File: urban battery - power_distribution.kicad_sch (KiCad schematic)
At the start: 19 parts, among them J1 FRONT_ACC_OUT, J2 12V_IN, J3 12VHC_OUT_EXTRA, J4 TEL_OUT, J5 REAR_ACC_OUT, J6 MTR_CTRL_OUT, J7 12VLC_OUT_EXTRA, J8 12VLC_OUT_EXTRA, J9 12VLC_OUT_EXTRA

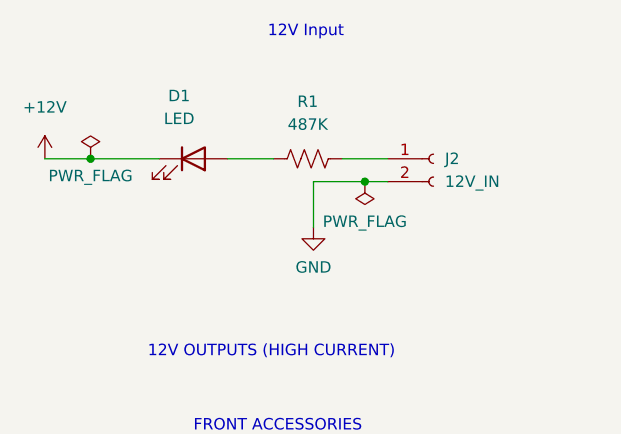
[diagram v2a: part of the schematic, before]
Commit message: fixed issue od 12V input going through LED
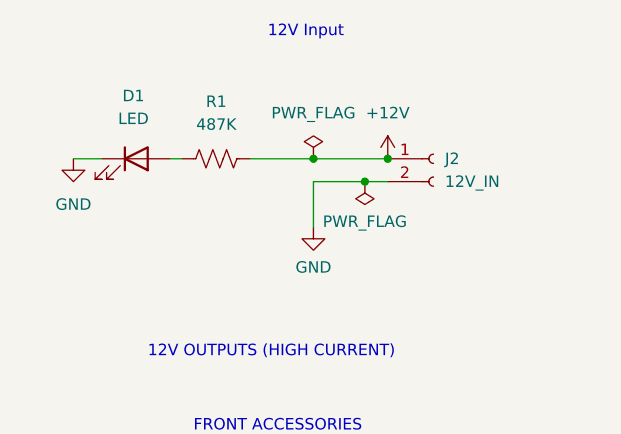
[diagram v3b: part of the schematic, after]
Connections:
- net +12V: now also J2.1 (Pin_1), R1.2; no longer D1.1 (K)
- net GND: now also D1.1 (K)
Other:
- moved on the sheet: D1, R1
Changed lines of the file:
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@@
 (kicad_sch (version 20211123) (generator eeschema)
   (paper "A4")
+  (junction (at 70.485 59.69) (diameter 0) (color 0 0 0 0)
+  )
   (junction (at 76.2 62.23) (diameter 0) (color 0 0 0 0)
   )
-  (junction (at 45.72 59.69) (diameter 0) (color 0 0 0 0)
+  (junction (at 78.74 59.69) (diameter 0) (color 0 0 0 0)
   )
   (wire (pts (xy 144.145 131.445) (xy 140.97 131.445))
@@
     (stroke (width 0) (type default) (color 0 0 0 0))
   )
-  (wire (pts (xy 73.66 59.69) (xy 78.74 59.69))
+  (wire (pts (xy 43.815 59.69) (xy 46.99 59.69))
     (stroke (width 0) (type default) (color 0 0 0 0))
   )
@@
     (stroke (width 0) (type default) (color 0 0 0 0))
   )
-  (wire (pts (xy 40.64 59.69) (xy 45.72 59.69))
-    (stroke (width 0) (type default) (color 0 0 0 0))
-  )
   (wire (pts (xy 53.975 102.235) (xy 53.975 107.315))
     (stroke (width 0) (type default) (color 0 0 0 0))
   )
-  (wire (pts (xy 45.72 59.69) (xy 53.34 59.69))
-    (stroke (width 0) (type default) (color 0 0 0 0))
-  )
   (wire (pts (xy 62.23 136.525) (xy 59.055 136.525))
     (stroke (width 0) (type default) (color 0 0 0 0))
   )
+  (wire (pts (xy 70.485 59.69) (xy 78.74 59.69))
+    (stroke (width 0) (type default) (color 0 0 0 0))
+  )
   (wire (pts (xy 203.835 100.965) (xy 200.66 100.965))
     (stroke (width 0) (type default) (color 0 0 0 0))
   )
-  (wire (pts (xy 60.96 59.69) (xy 66.04 59.69))
+  (wire (pts (xy 54.61 59.69) (xy 55.88 59.69))
     (stroke (width 0) (type default) (color 0 0 0 0))
   )
@@
   )
   (wire (pts (xy 140.97 66.675) (xy 140.97 71.755))
+    (stroke (width 0) (type default) (color 0 0 0 0))
+  )
+  (wire (pts (xy 63.5 59.69) (xy 70.485 59.69))
     (stroke (width 0) (type default) (color 0 0 0 0))
   )
@@
     (pin "2")
   )
-  (symbol (lib_id "Device:LED") (at 57.15 59.69 0) (unit 1)
+  (symbol (lib_id "power:GND") (at 43.815 59.69 0) (unit 1)
+    (in_bom yes) (on_board yes) (fields_autoplaced)
+    (property "Reference" "#PWR0102" (id 0) (at 43.815 66.04 0)
+      (effects (font (size 1.27 1.27)) hide)
+    )
+    (property "Value" "GND" (id 1) (at 43.815 64.77 0))
+    (property "Footprint" "" (id 2) (at 43.815 59.69 0)
+      (effects (font (size 1.27 1.27)) hide)
+    )
+    (property "Datasheet" "" (id 3) (at 43.815 59.69 0)
+      (effects (font (size 1.27 1.27)) hide)
+    )
+    (pin "1")
+  )
+  (symbol (lib_id "Device:LED") (at 50.8 59.69 0) (unit 1)
     (in_bom yes) (on_board yes)
-    (property "Reference" "D1" (id 0) (at 55.5625 52.705 0))
-    (property "Value" "LED" (id 1) (at 55.5625 55.245 0))
-    (property "Footprint" "LED_SMD:LED_1206_3216Metric" (id 2) (at 57.15 59.69 0)
-      (effects (font (size 1.27 1.27)) hide)
-    )
-    (property "Datasheet" "https://optoelectronics.liteon.com/upload/download/DS22-2000-026/LTST-C150TBKT(0630).pdf" (id 3) (at 57.15 59.69 0)
+    (property "Reference" "D1" (id 0) (at 50.4825 52.705 0))
+    (property "Value" "LED" (id 1) (at 50.4825 55.245 0))
+    (property "Footprint" "LED_SMD:LED_1206_3216Metric" (id 2) (at 50.8 59.69 0)
+      (effects (font (size 1.27 1.27)) hide)
+    )
+    (property "Datasheet" "https://optoelectronics.liteon.com/upload/download/DS22-2000-026/LTST-C150TBKT(0630).pdf" (id 3) (at 50.8 59.69 0)
       (effects (font (size 1.27 1.27)) hide)
     )
@@
     )
     (property "Datasheet" "" (id 3) (at 71.12 109.855 0)
-      (effects (font (size 1.27 1.27)) hide)
-    )
-    (pin "1")
-  )
-  (symbol (lib_id "power:PWR_FLAG") (at 45.72 59.69 0) (unit 1)
-    (in_bom yes) (on_board yes)
-    (property "Reference" "#FLG01" (id 0) (at 45.72 57.785 0)
-      (effects (font (size 1.27 1.27)) hide)
-    )
-    (property "Value" "PWR_FLAG" (id 1) (at 45.72 61.595 0))
-    (property "Footprint" "" (id 2) (at 45.72 59.69 0)
-      (effects (font (size 1.27 1.27)) hide)
-    )
-    (property "Datasheet" "~" (id 3) (at 45.72 59.69 0)
       (effects (font (size 1.27 1.27)) hide)
     )
@@
     (pin "2")
   )
+  (symbol (lib_id "power:PWR_FLAG") (at 70.485 59.69 0) (unit 1)
+    (in_bom yes) (on_board yes) (fields_autoplaced)
+    (property "Reference" "#FLG0101" (id 0) (at 70.485 57.785 0)
+      (effects (font (size 1.27 1.27)) hide)
+    )
+    (property "Value" "PWR_FLAG" (id 1) (at 70.485 54.61 0))
+    (property "Footprint" "" (id 2) (at 70.485 59.69 0)
+      (effects (font (size 1.27 1.27)) hide)
+    )
+    (property "Datasheet" "~" (id 3) (at 70.485 59.69 0)
+      (effects (font (size 1.27 1.27)) hide)
+    )
+    (pin "1")
+  )
   (symbol (lib_id "power:+12V") (at 59.055 131.445 0) (unit 1)
     (in_bom yes) (on_board yes) (fields_autoplaced)
@@
     (pin "1")
   )
-  (symbol (lib_id "Device:R_US") (at 69.85 59.69 90) (unit 1)
-    (in_bom yes) (on_board yes) (fields_autoplaced)
-    (property "Reference" "R1" (id 0) (at 69.85 53.34 90))
-    (property "Value" "487K" (id 1) (at 69.85 55.88 90))
-    (property "Footprint" "Resistor_SMD:R_0805_2012Metric" (id 2) (at 70.104 58.674 90)
-      (effects (font (size 1.27 1.27)) hide)
-    )
-    (property "Datasheet" "https://www.yageo.com/upload/media/product/productsearch/datasheet/rchip/PYu-RC_Group_51_RoHS_L_12.pdf" (id 3) (at 69.85 59.69 0)
-      (effects (font (size 1.27 1.27)) hide)
-    )
-    (pin "1")
-    (pin "2")
-  )
-  (symbol (lib_id "power:+12V") (at 40.64 59.69 0) (unit 1)
-    (in_bom yes) (on_board yes) (fields_autoplaced)
-    (property "Reference" "#PWR01" (id 0) (at 40.64 63.5 0)
-      (effects (font (size 1.27 1.27)) hide)
-    )
-    (property "Value" "+12V" (id 1) (at 40.64 53.975 0))
-    (property "Footprint" "" (id 2) (at 40.64 59.69 0)
-      (effects (font (size 1.27 1.27)) hide)
-    )
-    (property "Datasheet" "" (id 3) (at 40.64 59.69 0)
-      (effects (font (size 1.27 1.27)) hide)
-    )
-    (pin "1")
+  (symbol (lib_id "Device:R_US") (at 59.69 59.69 90) (unit 1)
+    (in_bom yes) (on_board yes) (fields_autoplaced)
+    (property "Reference" "R1" (id 0) (at 59.69 53.34 90))
+    (property "Value" "487K" (id 1) (at 59.69 55.88 90))
+    (property "Footprint" "Resistor_SMD:R_0805_2012Metric" (id 2) (at 59.944 58.674 90)
+      (effects (font (size 1.27 1.27)) hide)
+    )
+    (property "Datasheet" "https://www.yageo.com/upload/media/product/productsearch/datasheet/rchip/PYu-RC_Group_51_RoHS_L_12.pdf" (id 3) (at 59.69 59.69 0)
+      (effects (font (size 1.27 1.27)) hide)
+    )
+    (pin "1")
+    (pin "2")
   )
   (symbol (lib_id "Device:Fuse") (at 207.645 100.965 90) (unit 1)
@@
     (pin "2")
   )
+  (symbol (lib_id "power:+12V") (at 78.74 59.69 0) (unit 1)
+    (in_bom yes) (on_board yes) (fields_autoplaced)
+    (property "Reference" "#PWR0101" (id 0) (at 78.74 63.5 0)
+      (effects (font (size 1.27 1.27)) hide)
+    )
+    (property "Value" "+12V" (id 1) (at 78.74 54.61 0))
+    (property "Footprint" "" (id 2) (at 78.74 59.69 0)
+      (effects (font (size 1.27 1.27)) hide)
+    )
+    (property "Datasheet" "" (id 3) (at 78.74 59.69 0)
+      (effects (font (size 1.27 1.27)) hide)
+    )
+    (pin "1")
+  )
   (symbol (lib_id "Connector:Conn_01x02_Female") (at 80.01 136.525 0) (unit 1)
     (in_bom yes) (on_board yes) (fields_autoplaced)
@@
   )
   (symbol_instances
-    (path "/452fe402-7807-4995-87a6-34b6befdd6a5"
-      (reference "#FLG01") (unit 1) (value "PWR_FLAG") (footprint "")
-    )
     (path "/0d95df46-a92d-4f91-aeac-7d54430508e4"
       (reference "#FLG02") (unit 1) (value "PWR_FLAG") (footprint "")
     )
-    (path "/cbde6c9a-c2d7-401b-83df-c8ef54444e01"
-      (reference "#PWR01") (unit 1) (value "+12V") (footprint "")
+    (path "/b5bc7921-a871-498e-b0ae-d067dd25a013"
+      (reference "#FLG0101") (unit 1) (value "PWR_FLAG") (footprint "")
     )
     (path "/99639659-ef88-4665-ac4c-a2487cd291d6"
@@
       (reference "#PWR018") (unit 1) (value "GND") (footprint "")
     )
+    (path "/e5cbaa6e-32d6-4a8e-a669-628ca35be01c"
+      (reference "#PWR0101") (unit 1) (value "+12V") (footprint "")
+    )
+    (path "/2819f571-c515-4148-8b6c-c2181295bb72"
+      (reference "#PWR0102") (unit 1) (value "GND") (footprint "")
+    )
     (path "/2d6e8602-341a-4e49-8f22-a4538a6c33d0"

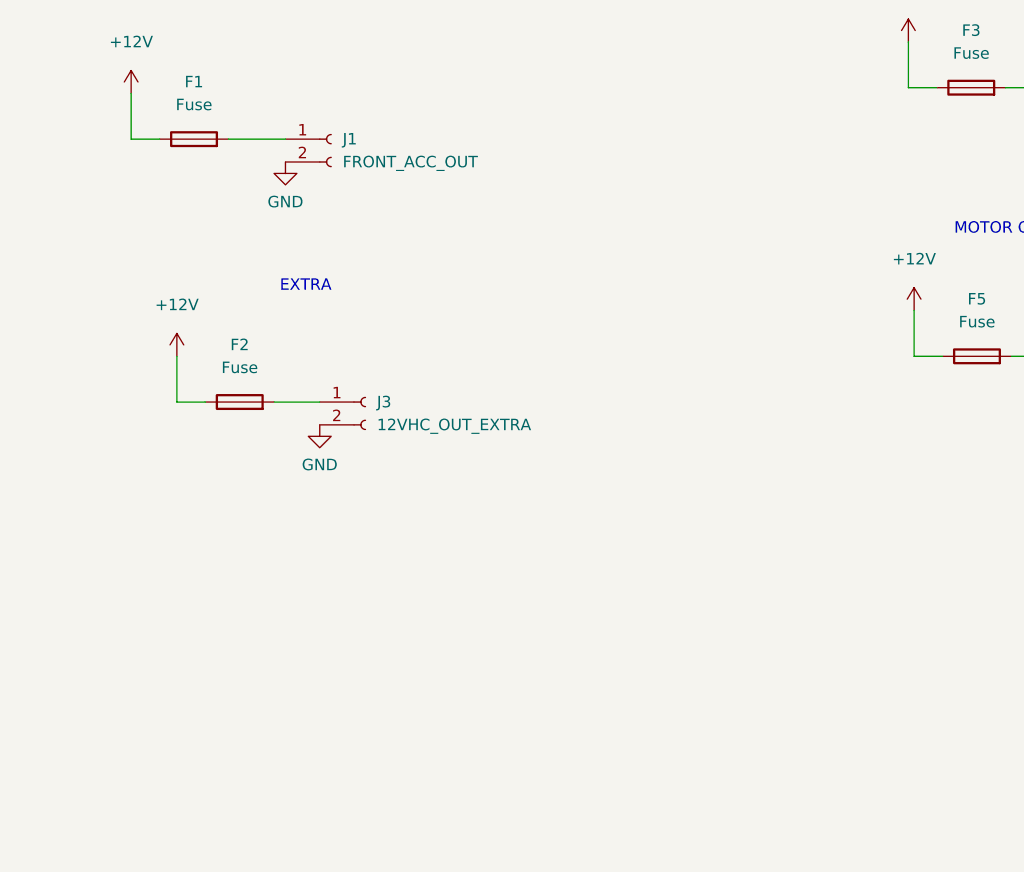
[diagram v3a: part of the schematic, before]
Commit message: pcb routing,added mounting holes and proper labels
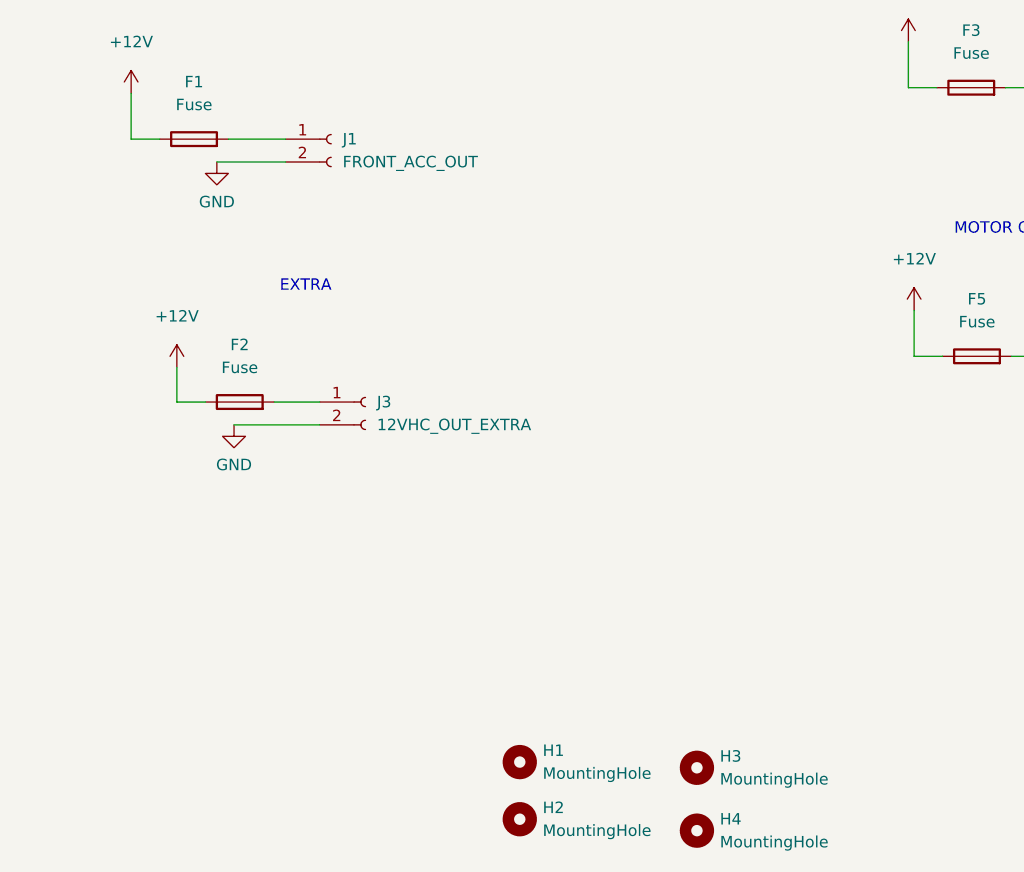
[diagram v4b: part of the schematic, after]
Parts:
- added H1, H2, H3, H4: MountingHole, MountingHole:MountingHole_3.2mm_M3, symbol Mechanical:MountingHole
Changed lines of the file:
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@@
+    (stroke (width 0) (type default) (color 0 0 0 0))
+  )
+  (wire (pts (xy 65.405 139.065) (xy 74.93 139.065))
     (stroke (width 0) (type default) (color 0 0 0 0))
   )
@@
     (stroke (width 0) (type default) (color 0 0 0 0))
   )
+  (wire (pts (xy 63.5 109.855) (xy 71.12 109.855))
+    (stroke (width 0) (type default) (color 0 0 0 0))
+  )
   (wire (pts (xy 140.97 126.365) (xy 140.97 131.445))
     (stroke (width 0) (type default) (color 0 0 0 0))
@@
     (stroke (width 0) (type default) (color 0 0 0 0))
   )
-  (wire (pts (xy 59.055 131.445) (xy 59.055 136.525))
+  (wire (pts (xy 59.055 132.715) (xy 59.055 136.525))
     (stroke (width 0) (type default) (color 0 0 0 0))
   )
@@
     (pin "1")
   )
-  (symbol (lib_id "power:GND") (at 71.12 109.855 0) (unit 1)
-    (in_bom yes) (on_board yes) (fields_autoplaced)
-    (property "Reference" "#PWR05" (id 0) (at 71.12 116.205 0)
-      (effects (font (size 1.27 1.27)) hide)
-    )
-    (property "Value" "GND" (id 1) (at 71.12 114.3 0))
-    (property "Footprint" "" (id 2) (at 71.12 109.855 0)
-      (effects (font (size 1.27 1.27)) hide)
-    )
-    (property "Datasheet" "" (id 3) (at 71.12 109.855 0)
+  (symbol (lib_id "power:GND") (at 63.5 109.855 0) (unit 1)
+    (in_bom yes) (on_board yes) (fields_autoplaced)
+    (property "Reference" "#PWR05" (id 0) (at 63.5 116.205 0)
+      (effects (font (size 1.27 1.27)) hide)
+    )
+    (property "Value" "GND" (id 1) (at 63.5 114.3 0))
+    (property "Footprint" "" (id 2) (at 63.5 109.855 0)
+      (effects (font (size 1.27 1.27)) hide)
+    )
+    (property "Datasheet" "" (id 3) (at 63.5 109.855 0)
       (effects (font (size 1.27 1.27)) hide)
     )
@@
     (pin "1")
   )
+  (symbol (lib_id "Mechanical:MountingHole") (at 97.155 176.53 0) (unit 1)
+    (in_bom yes) (on_board yes) (fields_autoplaced)
+    (property "Reference" "H1" (id 0) (at 99.695 175.2599 0)
+      (effects (font (size 1.27 1.27)) (justify left))
+    )
+    (property "Value" "MountingHole" (id 1) (at 99.695 177.7999 0)
+      (effects (font (size 1.27 1.27)) (justify left))
+    )
+    (property "Footprint" "MountingHole:MountingHole_3.2mm_M3" (id 2) (at 97.155 176.53 0)
+      (effects (font (size 1.27 1.27)) hide)
+    )
+    (property "Datasheet" "~" (id 3) (at 97.155 176.53 0)
+      (effects (font (size 1.27 1.27)) hide)
+    )
+  )
   (symbol (lib_id "power:+12V") (at 198.12 71.755 0) (unit 1)
     (in_bom yes) (on_board yes) (fields_autoplaced)
@@
     )
     (pin "1")
+  )
+  (symbol (lib_id "Mechanical:MountingHole") (at 97.155 182.88 0) (unit 1)
+    (in_bom yes) (on_board yes) (fields_autoplaced)
+    (property "Reference" "H2" (id 0) (at 99.695 181.6099 0)
+      (effects (font (size 1.27 1.27)) (justify left))
+    )
+    (property "Value" "MountingHole" (id 1) (at 99.695 184.1499 0)
+      (effects (font (size 1.27 1.27)) (justify left))
+    )
+    (property "Footprint" "MountingHole:MountingHole_3.2mm_M3" (id 2) (at 97.155 182.88 0)
+      (effects (font (size 1.27 1.27)) hide)
+    )
+    (property "Datasheet" "~" (id 3) (at 97.155 182.88 0)
+      (effects (font (size 1.27 1.27)) hide)
+    )
+  )
+  (symbol (lib_id "Mechanical:MountingHole") (at 116.84 177.165 0) (unit 1)
+    (in_bom yes) (on_board yes) (fields_autoplaced)
+    (property "Reference" "H3" (id 0) (at 119.38 175.8949 0)
+      (effects (font (size 1.27 1.27)) (justify left))
+    )
+    (property "Value" "MountingHole" (id 1) (at 119.38 178.4349 0)
+      (effects (font (size 1.27 1.27)) (justify left))
+    )
+    (property "Footprint" "MountingHole:MountingHole_3.2mm_M3" (id 2) (at 116.84 177.165 0)
+      (effects (font (size 1.27 1.27)) hide)
+    )
+    (property "Datasheet" "~" (id 3) (at 116.84 177.165 0)
+      (effects (font (size 1.27 1.27)) hide)
+    )
   )
   (symbol (lib_id "power:+12V") (at 53.975 102.235 0) (unit 1)
@@
     (pin "1")
   )
-  (symbol (lib_id "power:+12V") (at 59.055 131.445 0) (unit 1)
-    (in_bom yes) (on_board yes) (fields_autoplaced)
-    (property "Reference" "#PWR03" (id 0) (at 59.055 135.255 0)
-      (effects (font (size 1.27 1.27)) hide)
-    )
-    (property "Value" "+12V" (id 1) (at 59.055 125.73 0))
-    (property "Footprint" "" (id 2) (at 59.055 131.445 0)
-      (effects (font (size 1.27 1.27)) hide)
-    )
-    (property "Datasheet" "" (id 3) (at 59.055 131.445 0)
-      (effects (font (size 1.27 1.27)) hide)
-    )
-    (pin "1")
-  )
-  (symbol (lib_id "power:GND") (at 74.93 139.065 0) (unit 1)
-    (in_bom yes) (on_board yes) (fields_autoplaced)
-    (property "Reference" "#PWR06" (id 0) (at 74.93 145.415 0)
-      (effects (font (size 1.27 1.27)) hide)
-    )
-    (property "Value" "GND" (id 1) (at 74.93 143.51 0))
-    (property "Footprint" "" (id 2) (at 74.93 139.065 0)
-      (effects (font (size 1.27 1.27)) hide)
-    )
-    (property "Datasheet" "" (id 3) (at 74.93 139.065 0)
+  (symbol (lib_id "power:+12V") (at 59.055 132.715 0) (unit 1)
+    (in_bom yes) (on_board yes) (fields_autoplaced)
+    (property "Reference" "#PWR03" (id 0) (at 59.055 136.525 0)
+      (effects (font (size 1.27 1.27)) hide)
+    )
+    (property "Value" "+12V" (id 1) (at 59.055 127 0))
+    (property "Footprint" "" (id 2) (at 59.055 132.715 0)
+      (effects (font (size 1.27 1.27)) hide)
+    )
+    (property "Datasheet" "" (id 3) (at 59.055 132.715 0)
+      (effects (font (size 1.27 1.27)) hide)
+    )
+    (pin "1")
+  )
+  (symbol (lib_id "power:GND") (at 65.405 139.065 0) (unit 1)
+    (in_bom yes) (on_board yes) (fields_autoplaced)
+    (property "Reference" "#PWR06" (id 0) (at 65.405 145.415 0)
+      (effects (font (size 1.27 1.27)) hide)
+    )
+    (property "Value" "GND" (id 1) (at 65.405 143.51 0))
+    (property "Footprint" "" (id 2) (at 65.405 139.065 0)
+      (effects (font (size 1.27 1.27)) hide)
+    )
+    (property "Datasheet" "" (id 3) (at 65.405 139.065 0)
       (effects (font (size 1.27 1.27)) hide)
     )
@@
     (pin "2")
   )
+  (symbol (lib_id "Mechanical:MountingHole") (at 116.84 184.15 0) (unit 1)
+    (in_bom yes) (on_board yes) (fields_autoplaced)
+    (property "Reference" "H4" (id 0) (at 119.38 182.8799 0)
+      (effects (font (size 1.27 1.27)) (justify left))
+    )
+    (property "Value" "MountingHole" (id 1) (at 119.38 185.4199 0)
+      (effects (font (size 1.27 1.27)) (justify left))
+    )
+    (property "Footprint" "MountingHole:MountingHole_3.2mm_M3" (id 2) (at 116.84 184.15 0)
+      (effects (font (size 1.27 1.27)) hide)
+    )
+    (property "Datasheet" "~" (id 3) (at 116.84 184.15 0)
+      (effects (font (size 1.27 1.27)) hide)
+    )
+  )
   (symbol (lib_id "Device:Fuse") (at 207.645 100.965 90) (unit 1)
     (in_bom yes) (on_board yes) (fields_autoplaced)
@@
       (reference "F8") (unit 1) (value "Fuse") (footprint "Fuse:Fuseholder_Blade_Mini_Keystone_3568")
     )
+    (path "/7ded1f44-01b0-48ab-9df2-261d3425a54e"
+      (reference "H1") (unit 1) (value "MountingHole") (footprint "MountingHole:MountingHole_3.2mm_M3")
+    )
+    (path "/943fa81b-5e80-4fc7-8cc0-2f6430e69cb7"
+      (reference "H2") (unit 1) (value "MountingHole") (footprint "MountingHole:MountingHole_3.2mm_M3")
+    )
+    (path "/978647d5-c0bc-48a8-9c14-521d2789a3c2"
+      (reference "H3") (unit 1) (value "MountingHole") (footprint "MountingHole:MountingHole_3.2mm_M3")
+    )
+    (path "/de2f7f65-a407-4d54-bc38-1d880d70997b"
+      (reference "H4") (unit 1) (value "MountingHole") (footprint "MountingHole:MountingHole_3.2mm_M3")
+    )
     (path "/ffaacf94-8060-464b-8e0a-8714b7727bc4"
